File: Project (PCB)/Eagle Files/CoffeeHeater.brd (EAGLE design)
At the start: 152.4 x 97 mm, 40 parts, among them Q1 BSS138, U1 POCKETBEAGLE, U2 0.56_HEX_BACKPACK, U3 TPS63060

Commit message: Updated connections
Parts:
- moved D1 30.0 mm to (113.5, 84.7), turned to 270 degrees
- moved C7 28.7 mm to (108.0, 78.4), turned to 180 degrees
- moved R8 26.3 mm to (119.6, 84.7), turned to 0 degrees
- moved C6 21.9 mm to (108.0, 81.5), turned to 180 degrees
- moved L1 21.1 mm to (102.2, 67.8), turned to 90 degrees
- moved R7 18.0 mm to (113.5, 81.5)
- moved C5 15.2 mm to (108.0, 84.7), turned to 180 degrees
- moved Q1 14.0 mm to (127.0, 83.7), turned to 0 degrees
- moved C8 13.3 mm to (108.0, 75.2), turned to 180 degrees
- moved R3 6.31 mm to (40.9, 47.0)
- moved R6 5.67 mm to (118.5, 75.2), turned to 180 degrees
- moved R5 3.41 mm to (113.5, 75.2), turned to 180 degrees
- moved C4 2.52 mm to (118.5, 77.6)
- moved C3 2.34 mm to (118.4, 68.3), turned to 270 degrees
- moved R4 0.40 mm to (69.7, 87.8), flipped to the bottom, turned to 0 degrees
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- renumbered U$3 to D2
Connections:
- net I2C_SCL: no longer R3.1
- net I2C_SDA: now also R3.1
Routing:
- net 5.0V: track 232.7 -> 0.00 mm
- net VDD_5V: track 97.8 -> 0.00 mm
- net 12V_VIN: track 68.2 -> 0.00 mm
- net GND: track 66.4 -> 42.5 mm, vias 22 -> 18
- net N$6: track 29.2 -> 8.32 mm
- net N$1: track 20.8 -> 0.00 mm
- net PG: track 30.2 -> 44.9 mm
- net N$7: track 22.6 -> 8.32 mm
- net N$10: track 9.18 -> 4.10 mm
- net TEMP: track 41.5 -> 36.5 mm
- net N$2: track 75.0 -> 76.7 mm
- net N$9: track 14.0 -> 12.6 mm
- net BASE: track 12.7 -> 14.0 mm
- net START_0: track 101.6 -> 100.4 mm
- net I2C_SCL: track 32.2 -> 33.3 mm
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- added copper zone on layer 1, net 12V_VIN
- added copper zone on layer 1, net 5.0V
- added copper zone on layer 1, net N$1
- added copper zone on layer 16, net VDD_5V

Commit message: Updated library and created BOM
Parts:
- renumbered U$1 to T1, U$2 to TR1, U$4 to H1
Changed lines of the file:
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@@
 <attribute name="VALUE" x="58.42" y="9.652" size="1.27" layer="28" rot="MR0"/>
 </element>
-<element name="U$1" library="CoffeeHeater" package="DS18B20_TEMP_SENSOR" value="DS18B20_TEMP_SENSOR" x="77.47" y="78.74"/>
-<element name="U$2" library="CoffeeHeater" package="TIP32C_TRANSISTOR" value="TIP32C_TRANSISTOR" x="121.92" y="34.29"/>
+<element name="T1" library="CoffeeHeater" package="DS18B20_TEMP_SENSOR" value="DS18B20_TEMP_SENSOR" x="77.47" y="78.74"/>
+<element name="TR1" library="CoffeeHeater" package="TIP32C_TRANSISTOR" value="TIP32C_TRANSISTOR" x="121.92" y="34.29"/>
 <element name="D2" library="CoffeeHeater" package="DIODE" value="DIODE" x="104.648" y="34.29">
 <attribute name="NAME" x="103.378" y="35.306" size="0.8128" layer="25"/>
 <attribute name="VALUE" x="103.378" y="32.512" size="0.8128" layer="27"/>
 </element>
-<element name="U$4" library="CoffeeHeater" package="HEATING_PAD" value="HEATING_PAD" x="124.46" y="13.97"/>
+<element name="H1" library="CoffeeHeater" package="HEATING_PAD" value="HEATING_PAD" x="124.46" y="13.97"/>
 <element name="R4" library="ENGI301" package="R0603" value="2.2k" x="69.723" y="87.757" rot="MR0">
 <attribute name="NAME" x="70.739" y="88.773" size="0.8128" layer="26" rot="MR0"/>
@@
 <contactref element="U2" pad="VCC"/>
 <contactref element="R4" pad="1"/>
-<contactref element="U$1" pad="VDD"/>
+<contactref element="T1" pad="VDD"/>
 <polygon width="0.254" layer="16">
 <vertex x="44.069" y="68.834"/>
@@
 <contactref element="GREEN" pad="P$2"/>
 <contactref element="RED" pad="P$2"/>
-<contactref element="U$1" pad="GND"/>
+<contactref element="T1" pad="GND"/>
 <contactref element="U3" pad="7"/>
 <contactref element="U3" pad="THERMAL@7"/>
@@
 <vertex x="154.94" y="104.14"/>
 </polygon>
-<contactref element="U$4" pad="GND"/>
+<contactref element="H1" pad="GND"/>
 <via x="105.029" y="84.836" extent="1-16" drill="0.35"/>
 <via x="105.029" y="81.407" extent="1-16" drill="0.35"/>
@@
 <signal name="BASE">
 <contactref element="D2" pad="OUT"/>
-<contactref element="U$2" pad="B"/>
+<contactref element="TR1" pad="B"/>
 <wire x1="105.398" y1="34.29" x2="119.38" y2="34.29" width="0.254" layer="1"/>
 </signal>
@@
 </signal>
 <signal name="TEMP">
-<contactref element="U$1" pad="DQ"/>
+<contactref element="T1" pad="DQ"/>
 <contactref element="R4" pad="2"/>
 <contactref element="U1" pad="69"/>
@@
 <contactref element="C2" pad="1"/>
 <contactref element="X1" pad="2"/>
-<contactref element="U$2" pad="C"/>
+<contactref element="TR1" pad="C"/>
 <polygon width="0.254" layer="1">
 <vertex x="84.709" y="65.405"/>
@@
 </signal>
 <signal name="N$1">
-<contactref element="U$2" pad="E"/>
-<contactref element="U$4" pad="VDD"/>
+<contactref element="TR1" pad="E"/>
+<contactref element="H1" pad="VDD"/>
 <polygon width="0.254" layer="1">
 <vertex x="123.571" y="35.179"/>

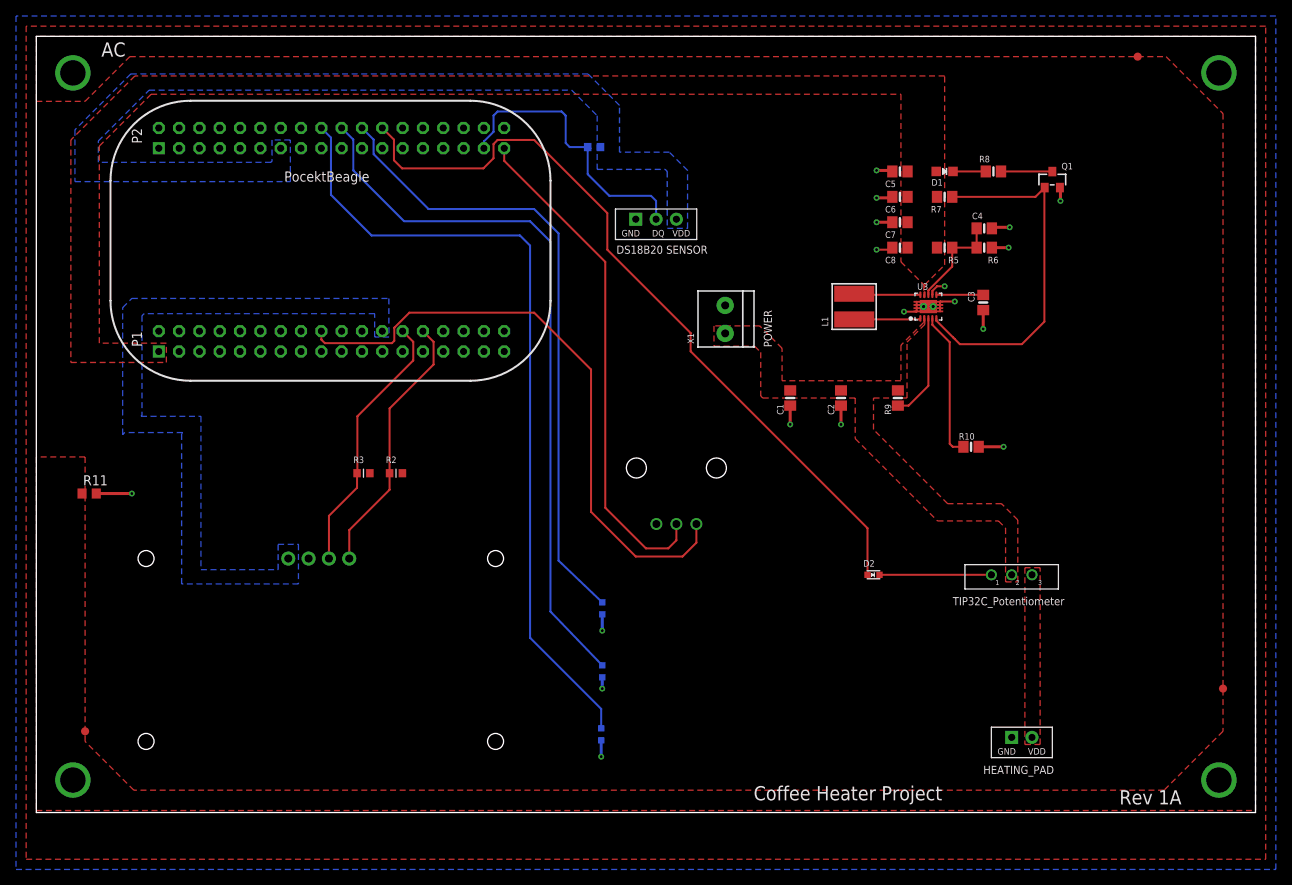
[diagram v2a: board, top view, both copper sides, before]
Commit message: Fixed pours and fixed gerber files
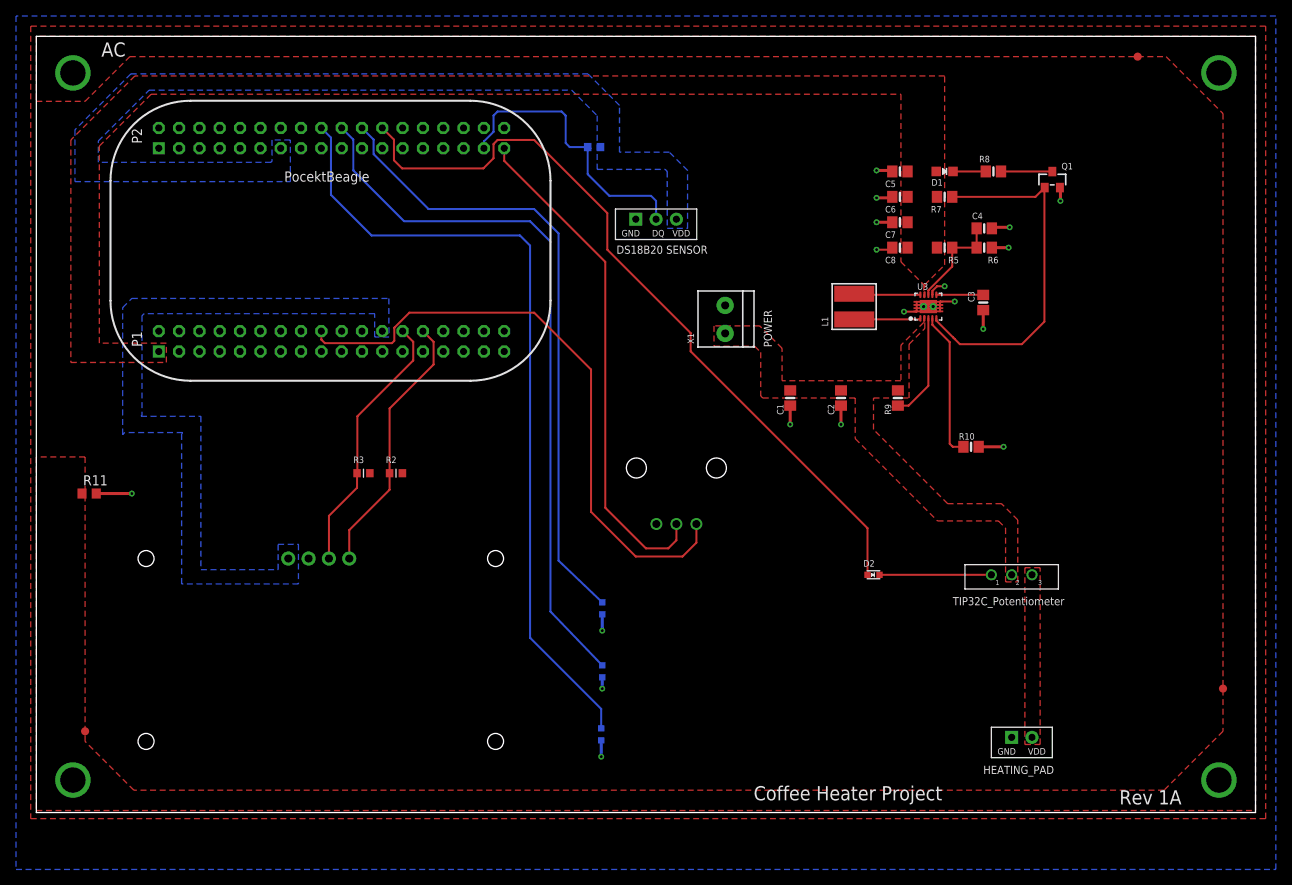
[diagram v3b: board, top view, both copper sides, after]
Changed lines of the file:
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@@
 <setting verticaltext="up"/>
 </settings>
-<grid distance="2.5" unitdist="mil" unit="mil" style="lines" multiple="1" display="yes" altdistance="5" altunitdist="mil" altunit="mil"/>
+<grid distance="10" unitdist="mil" unit="mil" style="lines" multiple="1" display="yes" altdistance="5" altunitdist="mil" altunit="mil"/>
 <layers>
 <layer number="1" name="Top" color="4" fill="1" visible="yes" active="yes"/>
@@
 <contactref element="R3" pad="2"/>
 <contactref element="R2" pad="2"/>
-<polygon width="0.1524" layer="1">
-<vertex x="-1.27" y="102.87"/>
-<vertex x="-1.27" y="-1.27"/>
-<vertex x="153.67" y="-1.27"/>
+<polygon width="0.254" layer="1" rank="6">
+<vertex x="-0.6985" y="102.87"/>
+<vertex x="-0.6985" y="3.81"/>
+<vertex x="153.67" y="3.81"/>
 <vertex x="153.67" y="102.87"/>
 </polygon>
@@
 <contactref element="Q1" pad="2"/>
 <contactref element="R10" pad="2"/>
-<polygon width="0.1524" layer="16">
+<polygon width="0.254" layer="16" rank="6">
 <vertex x="-2.54" y="104.14"/>
 <vertex x="-2.54" y="-2.54"/>
@@
 <contactref element="X1" pad="2"/>
 <contactref element="TR1" pad="C"/>
-<polygon width="0.254" layer="1">
+<polygon width="0.254" layer="1" rank="3">
 <vertex x="84.709" y="65.405"/>
 <vertex x="84.709" y="62.865"/>
@@
 <vertex x="104.648" y="52.451"/>
 <vertex x="104.648" y="56.388"/>
-<vertex x="108.839" y="56.388"/>
-<vertex x="108.839" y="63.373"/>
-<vertex x="111.0615" y="65.5955"/>
+<vertex x="109.093" y="56.388"/>
+<vertex x="109.093" y="63.119"/>
+<vertex x="111.0615" y="65.0875"/>
 <vertex x="111.0615" y="66.675"/>
 <vertex x="110.9345" y="66.675"/>
@@
 <vertex x="90.424" y="65.405"/>
 </polygon>
-<wire x1="107.696" y1="57.338" x2="111.006" y2="66.343" width="0" layer="19" extent="1-1"/>
 </signal>
 <signal name="N$1">
@@
 <contactref element="MGT3" pad="P$1"/>
 <contactref element="MGT2" pad="P$1"/>
-<polygon width="0.1524" layer="1">
+<polygon width="0.1524" layer="1" rank="2">
 <vertex x="0" y="93.472"/>
 <vertex x="6.096" y="93.472"/>
